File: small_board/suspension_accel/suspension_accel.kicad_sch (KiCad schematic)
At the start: 43 parts, among them IC1 TJA1050T_CM,118, IC2 AMS1117-3.3, IC3 SN74LVC1T45DCKR, IC4 ESP32-S3-MINI-1-N8, IC5 ADS1220IPWR, IC6 TLV75533PDBVR, IC7 SN74LVC1T45DCKR, J1 OSTTE040104, J2 BM04B-GVHS-TB_LF__SN_

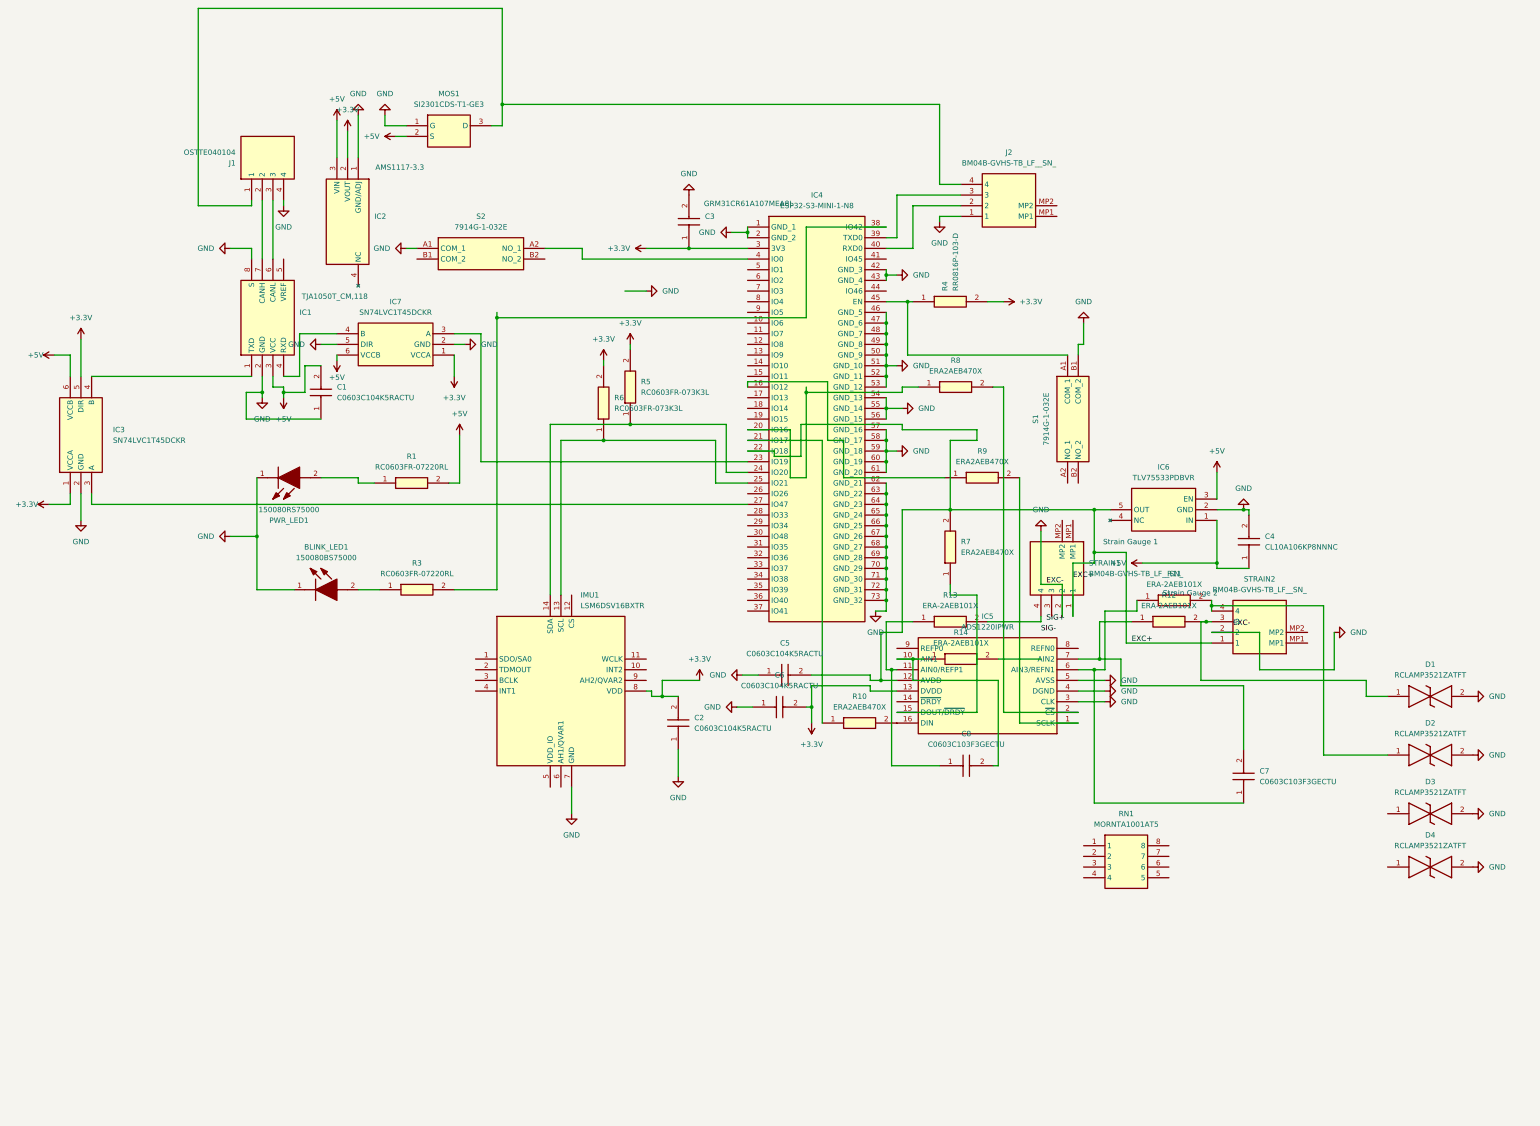
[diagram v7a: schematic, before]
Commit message: added ground pours and routed adc inputs
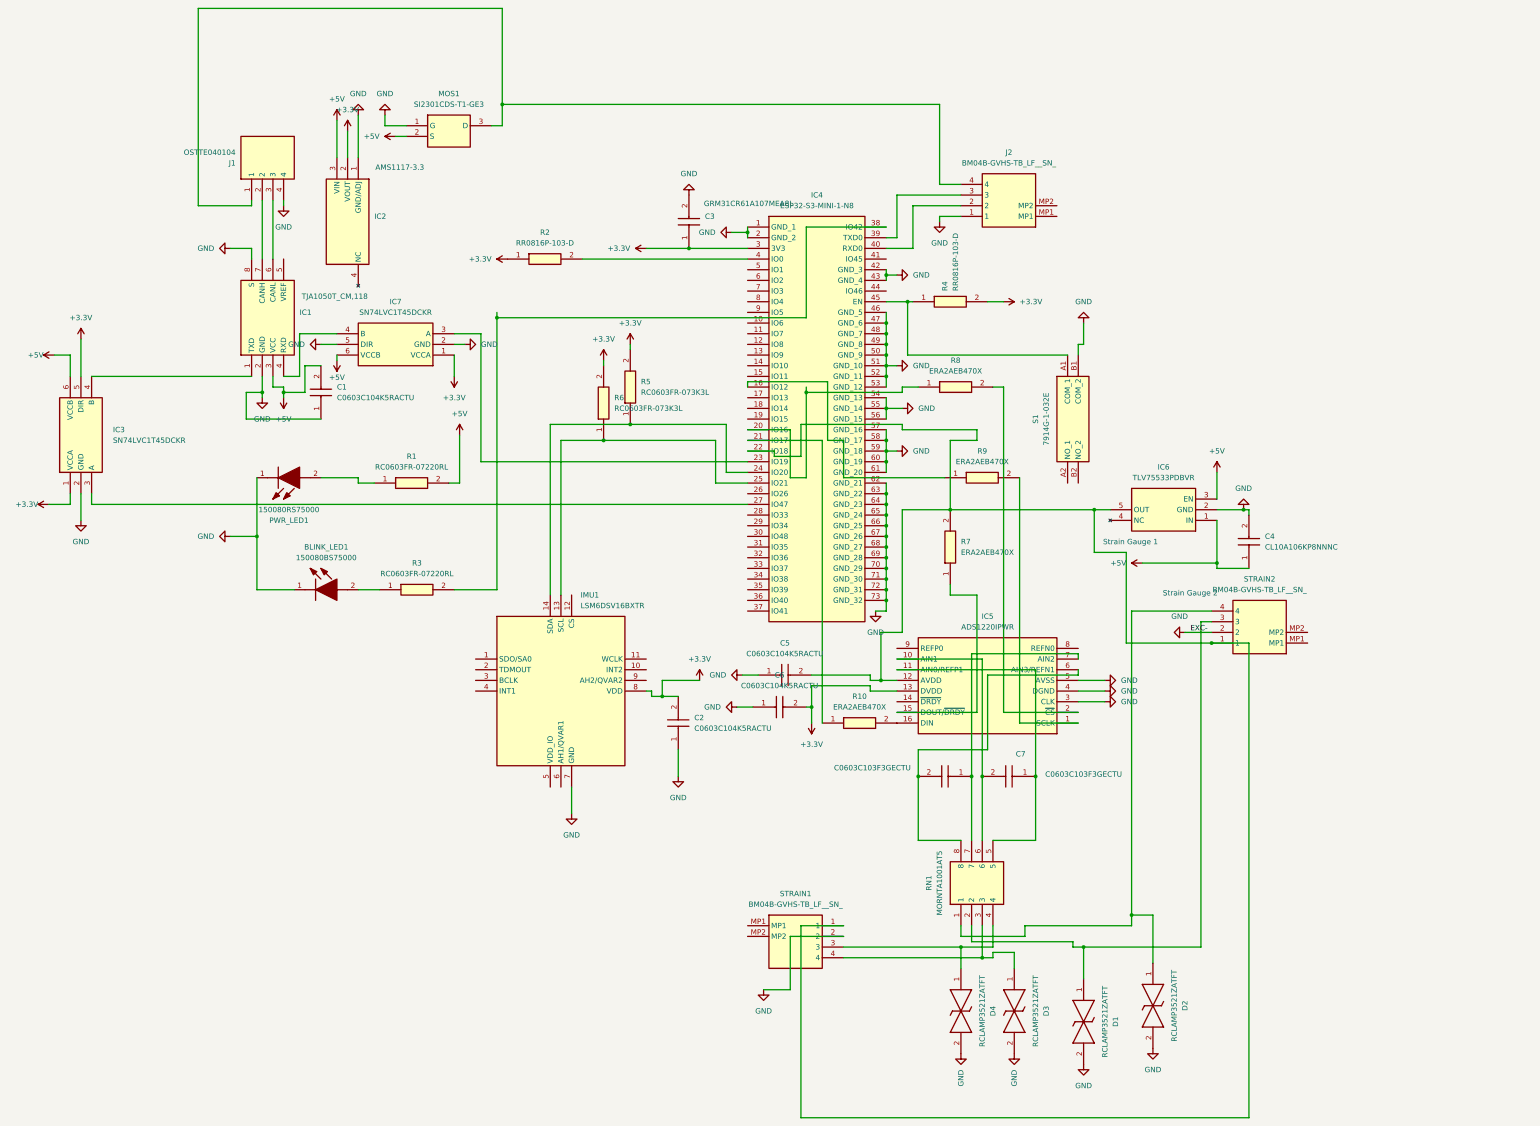
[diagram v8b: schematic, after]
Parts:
- removed R11, R12, R13, R14: ERA-2AEB101X, ERA2AED122X, symbol ERA-2AEB101X:ERA-2AEB101X
- removed S2: 7914G-1-032E, 7914G1032E, symbol 7914G-1-032E:7914G-1-032E
- added R2: RR0816P-103-D, RESC1608X60N, symbol RR0816P-103-D:RR0816P-103-D
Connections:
- net +3.3V: now also R2.1 (R1)
- net at C8.1: now also IC5.7 (AIN2), RN1.7; no longer IC5.11 (AIN0/REFP1)
- net at C8.2: now also IC5.6 (AIN3/REFN1), RN1.8; no longer IC5.10 (AIN1)
- net at C7.1: now also IC5.11 (AIN0/REFP1), RN1.5; no longer IC5.6 (AIN3/REFN1)
- net at C7.2: now also IC5.10 (AIN1), RN1.6; no longer IC5.7 (AIN2)
- net at STRAIN1.4: now also D3.1, RN1.3
- net at D1.1, STRAIN2.3: now also RN1.2
- net at IC4.4 (IO0): now also R2.2 (R2)
- net at D2.1, STRAIN2.4: now also RN1.1
- net at D4.1: now also RN1.4, STRAIN1.3
- net EXC+: no longer names the net of C5.2, IC4.22 (IO18), IC5.12 (AVDD), IC6.5 (OUT), R7.2, STRAIN1.1, STRAIN2.1
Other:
- moved on the sheet: C7, D1, D2, D3, D4, RN1, STRAIN1
